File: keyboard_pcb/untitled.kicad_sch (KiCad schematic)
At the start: 37 parts, among them J1 USB_C_Receptacle_USB2.0_16P, J2 Conn_01x02, J3 SWD, SW1 Reset, U1 XC6206PxxxMR, U2 RP2040, U3 W25Q128JVS, U4 74AHCT1G125, U5 SRV05-4, Y1 Crystal_GND24

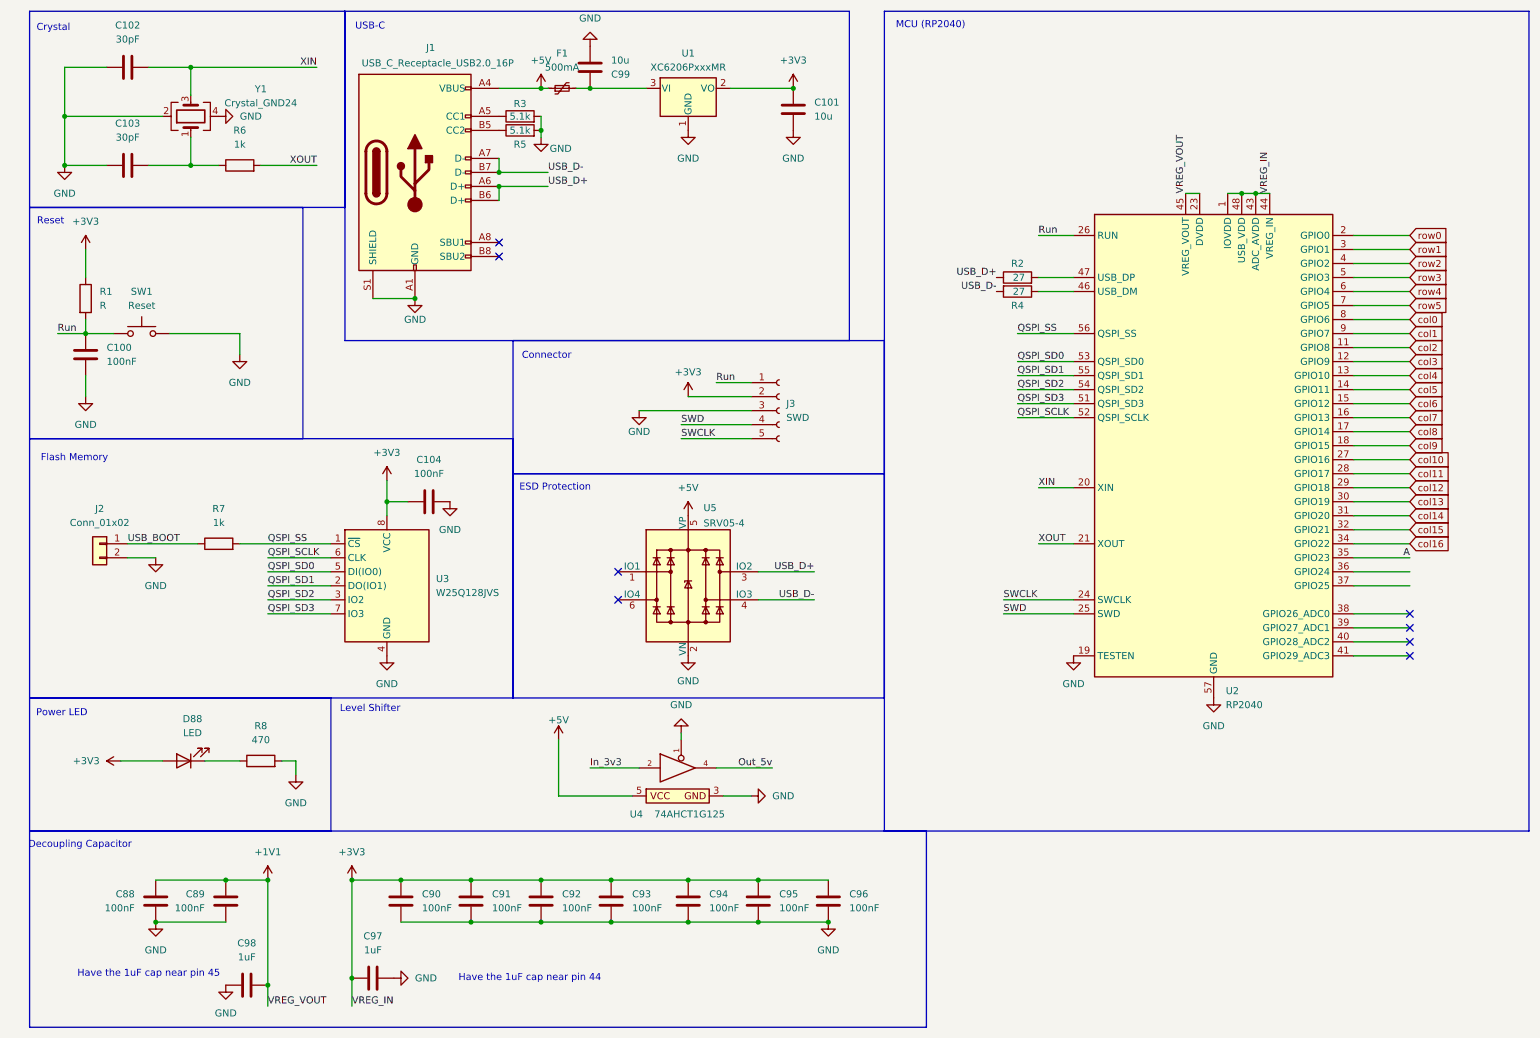
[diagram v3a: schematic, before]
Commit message: relocated the mcu to the shoulder
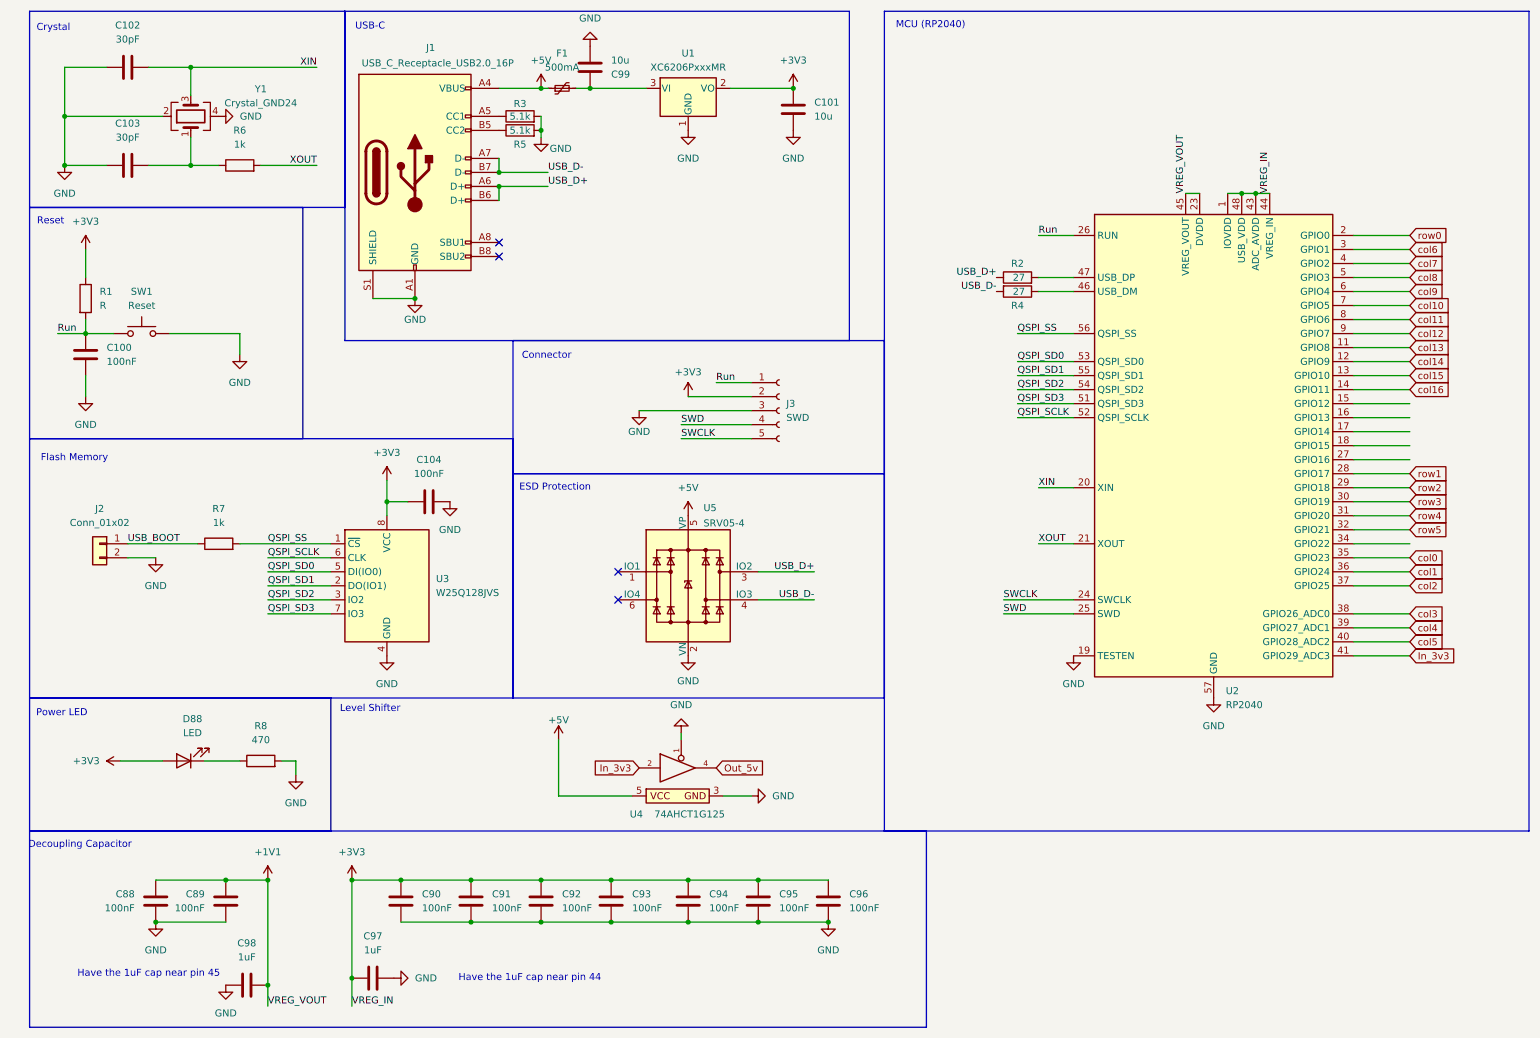
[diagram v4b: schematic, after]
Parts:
- C100, C101, C102, C103, C104, C88, C89, C90, C91, C92, C93, C94, C95, C96, C97, C98, C99: footprint Capacitor_SMD:C_0603_1608Metric_Pad1.08x0.95mm_HandSolder -> Capacitor_SMD:C_0402_1005Metric_Pad0.74x0.62mm_HandSolder
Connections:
- net A is gone; now on net col0: U2.35 (GPIO23)
- net In_3v3: now also U2.41 (GPIO29_ADC3)
- net col0: no longer U2.8 (GPIO6)
- net col1: now also U2.36 (GPIO24); no longer U2.9 (GPIO7)
- net col10: now also U2.7 (GPIO5); no longer U2.27 (GPIO16)
- net col11: now also U2.8 (GPIO6); no longer U2.28 (GPIO17)
- net col12: now also U2.9 (GPIO7); no longer U2.29 (GPIO18)
- net col13: now also U2.11 (GPIO8); no longer U2.30 (GPIO19)
- net col14: now also U2.12 (GPIO9); no longer U2.31 (GPIO20)
- net col15: now also U2.13 (GPIO10); no longer U2.32 (GPIO21)
- net col16: now also U2.14 (GPIO11); no longer U2.34 (GPIO22)
- net col2: now also U2.37 (GPIO25); no longer U2.11 (GPIO8)
- net col3: now also U2.38 (GPIO26_ADC0); no longer U2.12 (GPIO9)
- net col4: now also U2.39 (GPIO27_ADC1); no longer U2.13 (GPIO10)
- net col5: now also U2.40 (GPIO28_ADC2); no longer U2.14 (GPIO11)
- net col6: now also U2.3 (GPIO1); no longer U2.15 (GPIO12)
- net col7: now also U2.4 (GPIO2); no longer U2.16 (GPIO13)
- net col8: now also U2.5 (GPIO3); no longer U2.17 (GPIO14)
- net col9: now also U2.6 (GPIO4); no longer U2.18 (GPIO15)
- net row1: now also U2.28 (GPIO17); no longer U2.3 (GPIO1)
- net row2: now also U2.29 (GPIO18); no longer U2.4 (GPIO2)
- net row3: now also U2.30 (GPIO19); no longer U2.5 (GPIO3)
- net row4: now also U2.31 (GPIO20); no longer U2.6 (GPIO4)
- net row5: now also U2.32 (GPIO21); no longer U2.7 (GPIO5)
- no-connect marks 8 -> 4
